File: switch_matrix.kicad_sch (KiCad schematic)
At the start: 136 parts

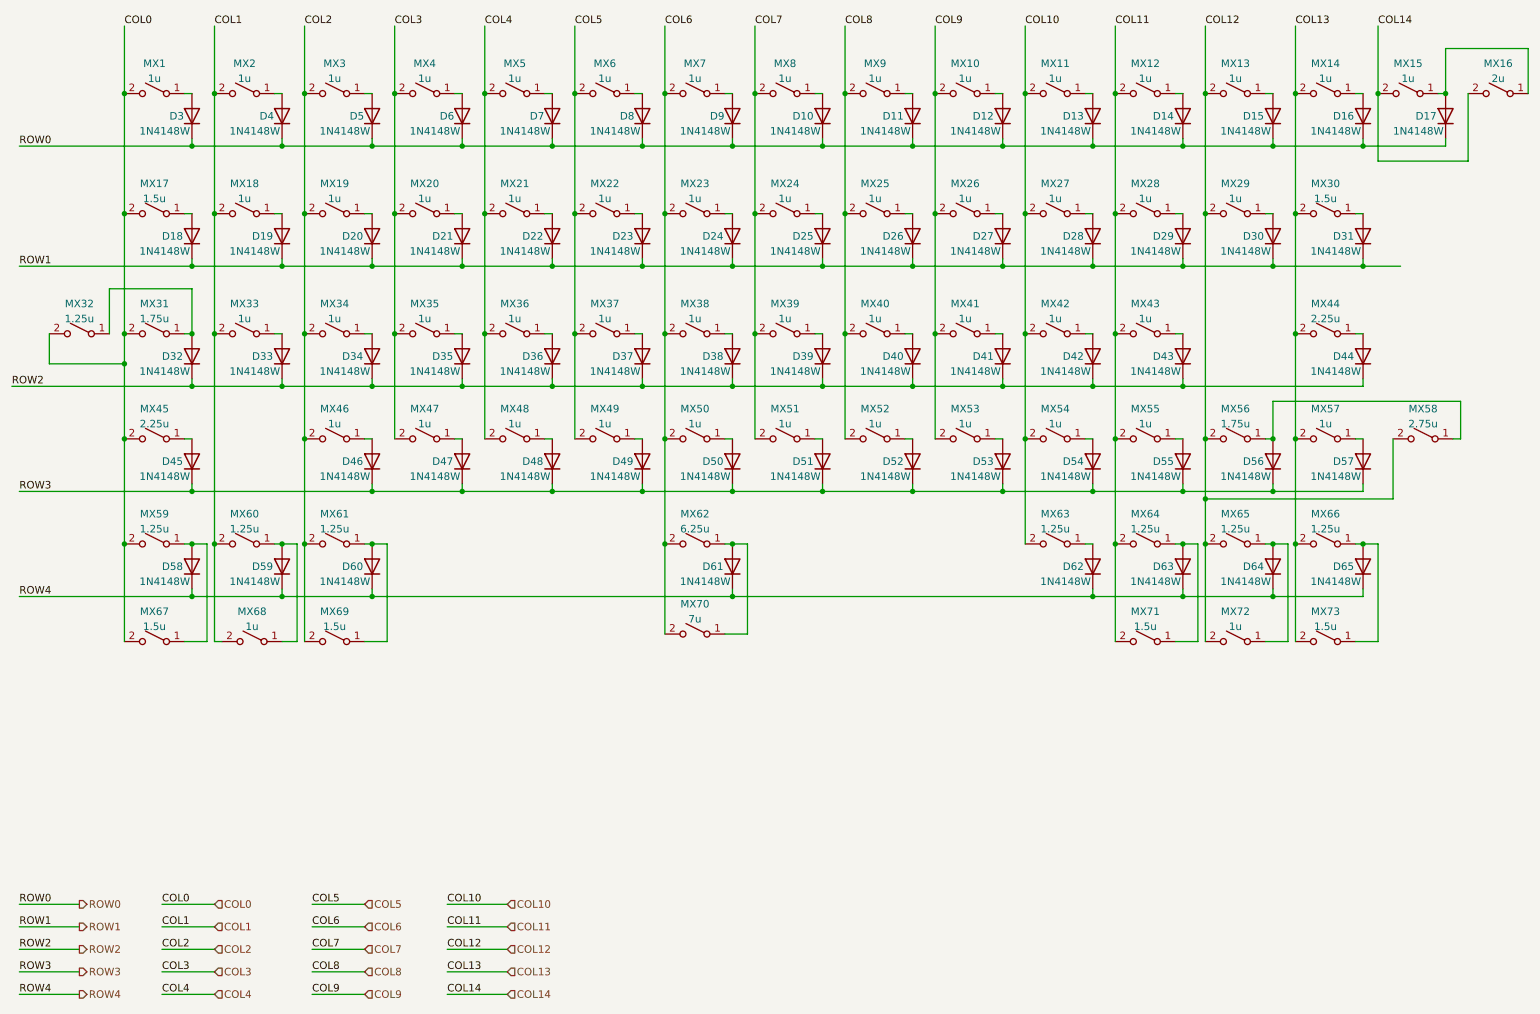
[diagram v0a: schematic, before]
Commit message: RGB and Keys added to sch
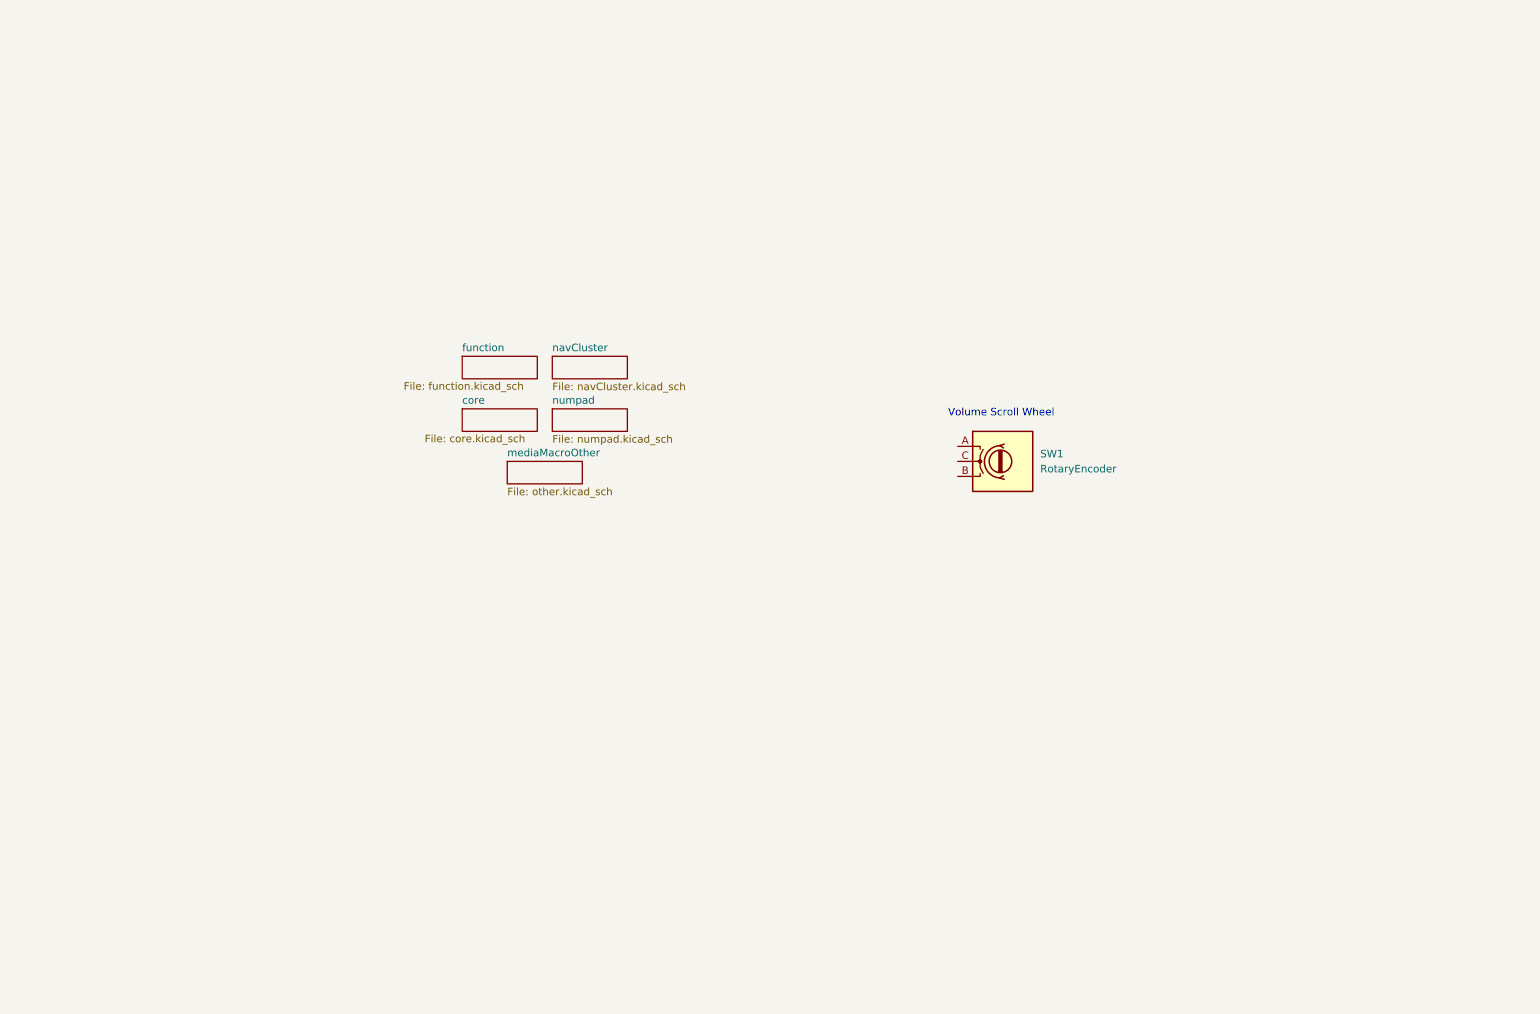
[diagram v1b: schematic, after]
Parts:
- removed D10, D11, D12, D13, D14, D15, D16, D17, D18, D19, D20, D21, D22, D23, D24, D25, D26, D27, D28, D29, D3, D30, D31, D32, D33, D34, D35, D36, D37, D38, D39, D4, D40, D41, D42, D43, D44, D45, D46, D47, D48, D49, D5, D50, D51, D52, D53, D54, D55, D56, D57, D58, D59, D6, D60, D61, D62, D63, D64, D65, D7, D8, D9: 1N4148W, keyboard:D_SOD-123, symbol keyboard:diode
- removed MX1, MX10, MX11, MX12, MX13, MX14, MX15, MX18, MX19, MX2, MX20, MX21, MX22, MX23, MX24, MX25, MX26, MX27, MX28, MX29, MX3, MX33, MX34, MX35, MX36, MX37, MX38, MX39, MX4, MX40, MX41, MX42, MX43, MX46, MX47, MX48, MX49, MX5, MX50, MX51, MX52, MX53, MX54, MX55, MX57, MX6, MX68, MX7, MX72, MX8, MX9: 1u, keyboard:SW_Cherry_MX_1.00u_PCB, symbol keyboard:switch
- removed MX16: 2u, keyboard:SW_Cherry_MX_2.00u_PCB, symbol keyboard:switch
- removed MX17, MX30, MX67, MX69, MX71, MX73: 1.5u, keyboard:SW_Cherry_MX_1.50u_PCB, symbol keyboard:switch
- removed MX31, MX56: 1.75u, keyboard:SW_Cherry_MX_1.75u_PCB, symbol keyboard:switch
- removed MX32, MX59, MX60, MX61, MX63, MX64, MX65, MX66: 1.25u, keyboard:SW_Cherry_MX_1.25u_PCB, symbol keyboard:switch
- removed MX44, MX45: 2.25u, keyboard:SW_Cherry_MX_2.25u_PCB, symbol keyboard:switch
- removed MX58: 2.75u, keyboard:SW_Cherry_MX_2.75u_PCB, symbol keyboard:switch
- removed MX62: 6.25u, keyboard:SW_Cherry_MX_6.25u_PCB, symbol keyboard:switch
- removed MX70: 7u, keyboard:SW_Cherry_MX_7.00u_PCB, symbol keyboard:switch
- added SW1: RotaryEncoder, symbol Device:RotaryEncoder
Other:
- added sheet core (core.kicad_sch)
- added sheet function (function.kicad_sch)
- added sheet mediaMacroOther (other.kicad_sch)
- added sheet navCluster (navCluster.kicad_sch)
- added sheet numpad (numpad.kicad_sch)
- note added: "Volume Scroll Wheel"

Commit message: Unified key sch pages
One large page is simpler in this case
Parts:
- removed SW1: RotaryEncoder, symbol Device:RotaryEncoder
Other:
- removed sheet core
- removed sheet function
- removed sheet mediaMacroOther
- removed sheet navCluster
- removed sheet numpad
- added sheet K_0 (key_rgb.kicad_sch)
- added sheet K_1 (key_rgb.kicad_sch)
- added sheet K_2 (key_rgb.kicad_sch)
- added sheet K_3 (key_rgb.kicad_sch)
- added sheet K_4 (key_rgb.kicad_sch)
- added sheet K_5 (key_rgb.kicad_sch)
- added sheet K_6 (key_rgb.kicad_sch)
- added sheet K_7 (key_rgb.kicad_sch)
- added sheet K_8 (key_rgb.kicad_sch)
- added sheet K_9 (key_rgb.kicad_sch)
- added sheet K_A (key_rgb.kicad_sch)
- added sheet K_Apostrophe (key_rgb.kicad_sch)
- added sheet K_B (key_rgb.kicad_sch)
- added sheet K_Backslash (key_rgb.kicad_sch)
- added sheet K_Backspace (key_rgb.kicad_sch)
- added sheet K_Bluetooth (key_rgb.kicad_sch)
- added sheet K_Brightness (key_rgb.kicad_sch)
- added sheet K_C (key_rgb.kicad_sch)
- added sheet K_CAPS (key_rgb.kicad_sch)
- added sheet K_Comma (key_rgb.kicad_sch)
- added sheet K_D (key_rgb.kicad_sch)
- added sheet K_DEL (key_rgb.kicad_sch)
- added sheet K_DOWN (key_rgb.kicad_sch)
- added sheet K_E (key_rgb.kicad_sch)
- added sheet K_END (key_rgb.kicad_sch)
- added sheet K_ENTER (key_rgb.kicad_sch)
- added sheet K_ESC (key_rgb.kicad_sch)
- added sheet K_Equals (key_rgb.kicad_sch)
- added sheet K_F (key_rgb.kicad_sch)
- added sheet K_F1 (key_rgb.kicad_sch)
- added sheet K_F10 (key_rgb.kicad_sch)
- added sheet K_F11 (key_rgb.kicad_sch)
- added sheet K_F12 (key_rgb.kicad_sch)
- added sheet K_F2 (key_rgb.kicad_sch)
- added sheet K_F3 (key_rgb.kicad_sch)
- added sheet K_F4 (key_rgb.kicad_sch)
- added sheet K_F5 (key_rgb.kicad_sch)
- added sheet K_F6 (key_rgb.kicad_sch)
- added sheet K_F7 (key_rgb.kicad_sch)
- added sheet K_F8 (key_rgb.kicad_sch)
- added sheet K_F9 (key_rgb.kicad_sch)
- added sheet K_G (key_rgb.kicad_sch)
- added sheet K_G1 (key_rgb.kicad_sch)
- added sheet K_G2 (key_rgb.kicad_sch)
- added sheet K_G3 (key_rgb.kicad_sch)
- added sheet K_G4 (key_rgb.kicad_sch)
- added sheet K_G5 (key_rgb.kicad_sch)
- added sheet K_GameMode (key_rgb.kicad_sch)
- added sheet K_H (key_rgb.kicad_sch)
- added sheet K_HOME (key_rgb.kicad_sch)
- added sheet K_I (key_rgb.kicad_sch)
- added sheet K_INS (key_rgb.kicad_sch)
- added sheet K_J (key_rgb.kicad_sch)
- added sheet K_K (key_rgb.kicad_sch)
- added sheet K_L (key_rgb.kicad_sch)
- added sheet K_LALT (key_rgb.kicad_sch)
- added sheet K_LBracket (key_rgb.kicad_sch)
- added sheet K_LCTRL (key_rgb.kicad_sch)
- added sheet K_LEFT (key_rgb.kicad_sch)
- added sheet K_LSHIFT (key_rgb.kicad_sch)
- added sheet K_LWin (key_rgb.kicad_sch)
- added sheet K_M (key_rgb.kicad_sch)
- added sheet K_M1 (key_rgb.kicad_sch)
- added sheet K_M2 (key_rgb.kicad_sch)
- added sheet K_M3 (key_rgb.kicad_sch)
- added sheet K_MR (key_rgb.kicad_sch)
- added sheet K_Menu (key_rgb.kicad_sch)
- added sheet K_Minus (key_rgb.kicad_sch)
- added sheet K_Mute (key_rgb.kicad_sch)
- added sheet K_N (key_rgb.kicad_sch)
- added sheet K_Next (key_rgb.kicad_sch)
- added sheet K_O (key_rgb.kicad_sch)
- added sheet K_P (key_rgb.kicad_sch)
- added sheet K_PAUSE (key_rgb.kicad_sch)
- added sheet K_PGDN (key_rgb.kicad_sch)
- added sheet K_PGUP (key_rgb.kicad_sch)
- added sheet K_PRTSC (key_rgb.kicad_sch)
- added sheet K_Period (key_rgb.kicad_sch)
- added sheet K_Play (key_rgb.kicad_sch)
- added sheet K_Prev (key_rgb.kicad_sch)
- added sheet K_Q (key_rgb.kicad_sch)
- added sheet K_R (key_rgb.kicad_sch)
- added sheet K_RALT (key_rgb.kicad_sch)
- added sheet K_RBracket (key_rgb.kicad_sch)
- added sheet K_RCTRL (key_rgb.kicad_sch)
- added sheet K_RIGHT (key_rgb.kicad_sch)
- added sheet K_RSHIFT (key_rgb.kicad_sch)
- added sheet K_RWIN (key_rgb.kicad_sch)
- added sheet K_S (key_rgb.kicad_sch)
- added sheet K_SCRLK (key_rgb.kicad_sch)
- added sheet K_Semicolon (key_rgb.kicad_sch)
- added sheet K_Slash (key_rgb.kicad_sch)
- added sheet K_Space (key_rgb.kicad_sch)
- added sheet K_T (key_rgb.kicad_sch)
- added sheet K_TABS (key_rgb.kicad_sch)
- added sheet K_Tilde (key_rgb.kicad_sch)
- added sheet K_U (key_rgb.kicad_sch)
- added sheet K_UP (key_rgb.kicad_sch)
- added sheet K_V (key_rgb.kicad_sch)
- added sheet K_W (key_rgb.kicad_sch)
- added sheet K_Wireless (key_rgb.kicad_sch)
- added sheet K_X (key_rgb.kicad_sch)
- added sheet K_Y (key_rgb.kicad_sch)
- added sheet K_Z (key_rgb.kicad_sch)
- added sheet K_np0 (key_rgb.kicad_sch)
- added sheet K_np1 (key_rgb.kicad_sch)
- added sheet K_np2 (key_rgb.kicad_sch)
- added sheet K_np3 (key_rgb.kicad_sch)
- added sheet K_np4 (key_rgb.kicad_sch)
- added sheet K_np5 (key_rgb.kicad_sch)
- added sheet K_np6 (key_rgb.kicad_sch)
- added sheet K_np7 (key_rgb.kicad_sch)
- added sheet K_np8 (key_rgb.kicad_sch)
- added sheet K_np9 (key_rgb.kicad_sch)
- added sheet K_npAsterisk (key_rgb.kicad_sch)
- added sheet K_npDecimal (key_rgb.kicad_sch)
- added sheet K_npEnter (key_rgb.kicad_sch)
- added sheet K_npMinus (key_rgb.kicad_sch)
- added sheet K_npNUM (key_rgb.kicad_sch)
- added sheet K_npPlus (key_rgb.kicad_sch)
- added sheet K_npSlash (key_rgb.kicad_sch)
- note removed: "Volume Scroll Wheel"

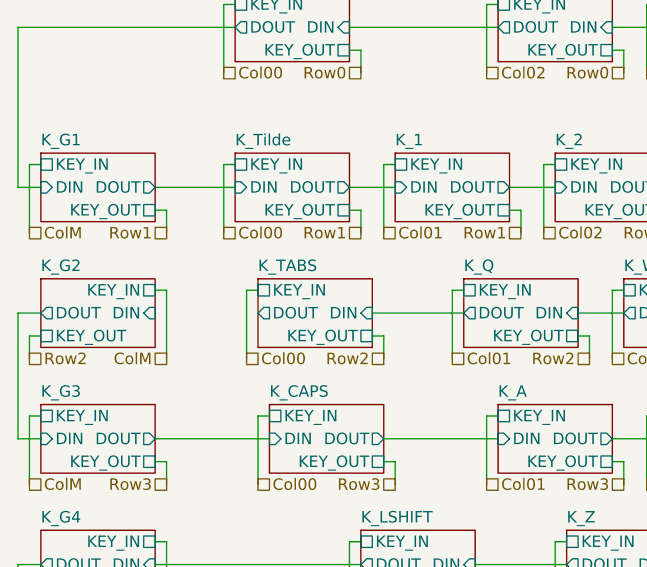
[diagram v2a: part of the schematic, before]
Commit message: Layout start. Add symbols to proj lib
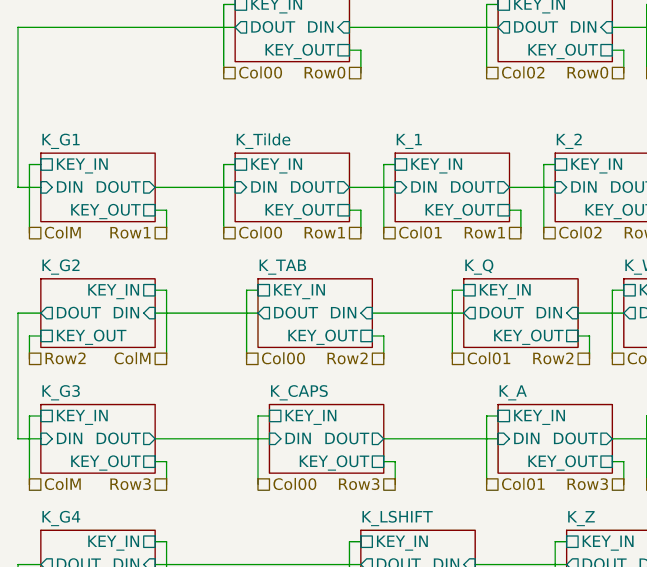
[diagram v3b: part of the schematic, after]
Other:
- sheet K_TABS renamed K_TAB

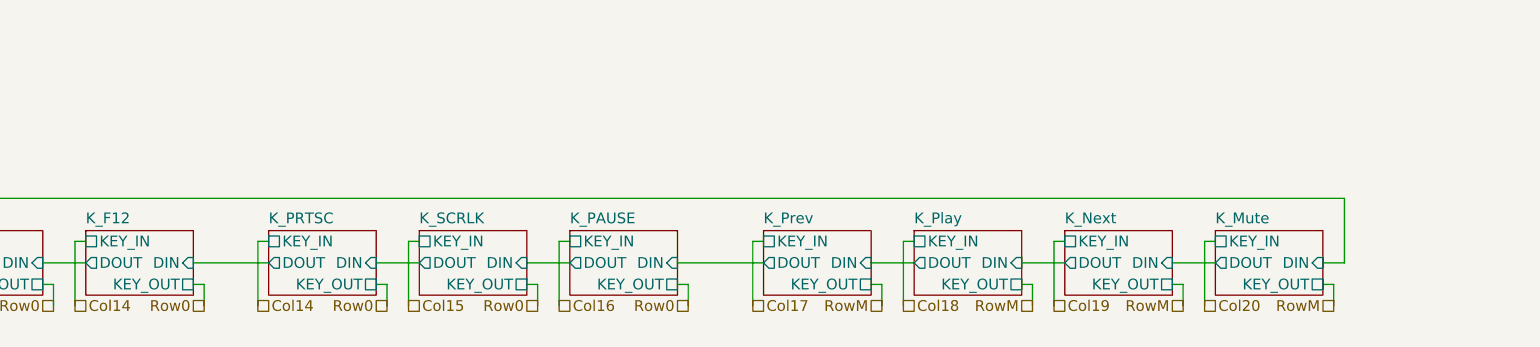
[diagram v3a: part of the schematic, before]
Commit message: Status LEDs
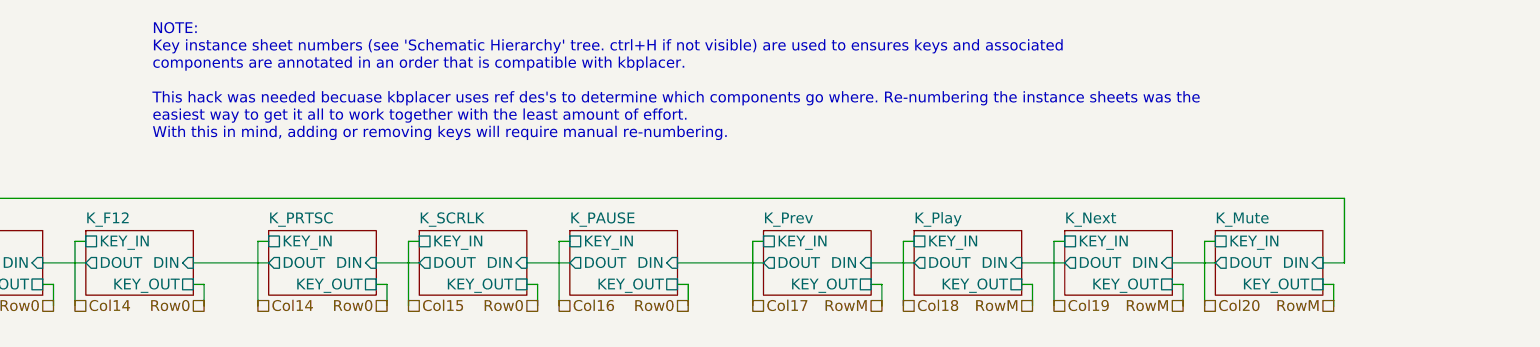
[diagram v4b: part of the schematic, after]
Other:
- note added: "NOTE: Key instance sheet numbers (see 'Schematic Hierarchy' tree. ctrl+H if not visible) are used to ensures keys and associated components are annotated in an order that is compatible with kbplacer. This hack was needed becuase kbplacer uses ref des's to determine which components go where. Re-numbering the instance sheets was the easiest way to get it all to work together with the least amount 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"
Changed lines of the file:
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@@
 		(company "HW-tinkerers")
+	)
+	(text "NOTE:\nKey instance sheet numbers (see 'Schematic Hierarchy' tree. ctrl+H if not visible) are used to ensures keys and associated\ncomponents are annotated in an order that is compatible with kbplacer.\n\nThis hack was needed becuase kbplacer uses ref des's to determine which components go where. Re-numbering the instance sheets was the\neasiest way to get it all to work together with the least amount of effort.\nWith this in mind, adding or removing keys will require manual re-numbering."
+		(exclude_from_sim no)
+		(at 294.894 21.844 0)
+		(effects
+			(font
+				(size 1.27 1.27)
+			)
+			(justify left)
+		)
 	)
 	(wire

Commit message: Minor sch changes. Work towards matching g915 pcb dimensions
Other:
- sheet K_Bluetooth: file key_rgb.kicad_sch -> key-mem_rgb.kicad_sch
- sheet K_Brightness: file key_rgb.kicad_sch -> key-mem_rgb.kicad_sch
- sheet K_GameMode: file key_rgb.kicad_sch -> key-mem_rgb.kicad_sch
- sheet K_M1: file key_rgb.kicad_sch -> key-mem_rgb.kicad_sch
- sheet K_M2: file key_rgb.kicad_sch -> key-mem_rgb.kicad_sch
- sheet K_M3: file key_rgb.kicad_sch -> key-mem_rgb.kicad_sch
- sheet K_MR: file key_rgb.kicad_sch -> key-mem_rgb.kicad_sch
- sheet K_Mute: file key_rgb.kicad_sch -> key-mem_rgb.kicad_sch
- sheet K_Next: file key_rgb.kicad_sch -> key-mem_rgb.kicad_sch
- sheet K_Play: file key_rgb.kicad_sch -> key-mem_rgb.kicad_sch
- sheet K_Prev: file key_rgb.kicad_sch -> key-mem_rgb.kicad_sch
- sheet K_Wireless: file key_rgb.kicad_sch -> key-mem_rgb.kicad_sch
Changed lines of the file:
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@@
 			)
 		)
-		(property "Sheetfile" "key_rgb.kicad_sch"
+		(property "Sheetfile" "key-mem_rgb.kicad_sch"
 			(at 367.03 47.5746 0)
 			(effects
@@
 			)
 		)
-		(property "Sheetfile" "key_rgb.kicad_sch"
+		(property "Sheetfile" "key-mem_rgb.kicad_sch"
 			(at 167.64 29.7946 0)
 			(effects
@@
 			)
 		)
-		(property "Sheetfile" "key_rgb.kicad_sch"
+		(property "Sheetfile" "key-mem_rgb.kicad_sch"
 			(at 384.81 47.5746 0)
 			(effects
@@
 			)
 		)
-		(property "Sheetfile" "key_rgb.kicad_sch"
+		(property "Sheetfile" "key-mem_rgb.kicad_sch"
 			(at 67.31 29.7946 0)
 			(effects
@@
 			)
 		)
-		(property "Sheetfile" "key_rgb.kicad_sch"
+		(property "Sheetfile" "key-mem_rgb.kicad_sch"
 			(at 203.2 29.7946 0)
 			(effects
@@
 			)
 		)
-		(property "Sheetfile" "key_rgb.kicad_sch"
+		(property "Sheetfile" "key-mem_rgb.kicad_sch"
 			(at 402.59 47.5746 0)
 			(effects
@@
 			)
 		)
-		(property "Sheetfile" "key_rgb.kicad_sch"
+		(property "Sheetfile" "key-mem_rgb.kicad_sch"
 			(at 85.09 29.7946 0)
 			(effects
@@
 			)
 		)
-		(property "Sheetfile" "key_rgb.kicad_sch"
+		(property "Sheetfile" "key-mem_rgb.kicad_sch"
 			(at 102.87 29.7946 0)
 			(effects
@@
 			)
 		)
-		(property "Sheetfile" "key_rgb.kicad_sch"
+		(property "Sheetfile" "key-mem_rgb.kicad_sch"
 			(at 149.86 29.7946 0)
 			(effects
@@
 			)
 		)
-		(property "Sheetfile" "key_rgb.kicad_sch"
+		(property "Sheetfile" "key-mem_rgb.kicad_sch"
 			(at 420.37 47.5746 0)
 			(effects
@@
 			)
 		)
-		(property "Sheetfile" "key_rgb.kicad_sch"
+		(property "Sheetfile" "key-mem_rgb.kicad_sch"
 			(at 185.42 29.7946 0)
 			(effects
@@
 			)
 		)
-		(property "Sheetfile" "key_rgb.kicad_sch"
+		(property "Sheetfile" "key-mem_rgb.kicad_sch"
 			(at 120.65 29.7946 0)
 			(effects
